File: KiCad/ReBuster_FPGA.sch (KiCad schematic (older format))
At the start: 25 parts, among them U1 10M02SCU169, U2 LM1117-3.3

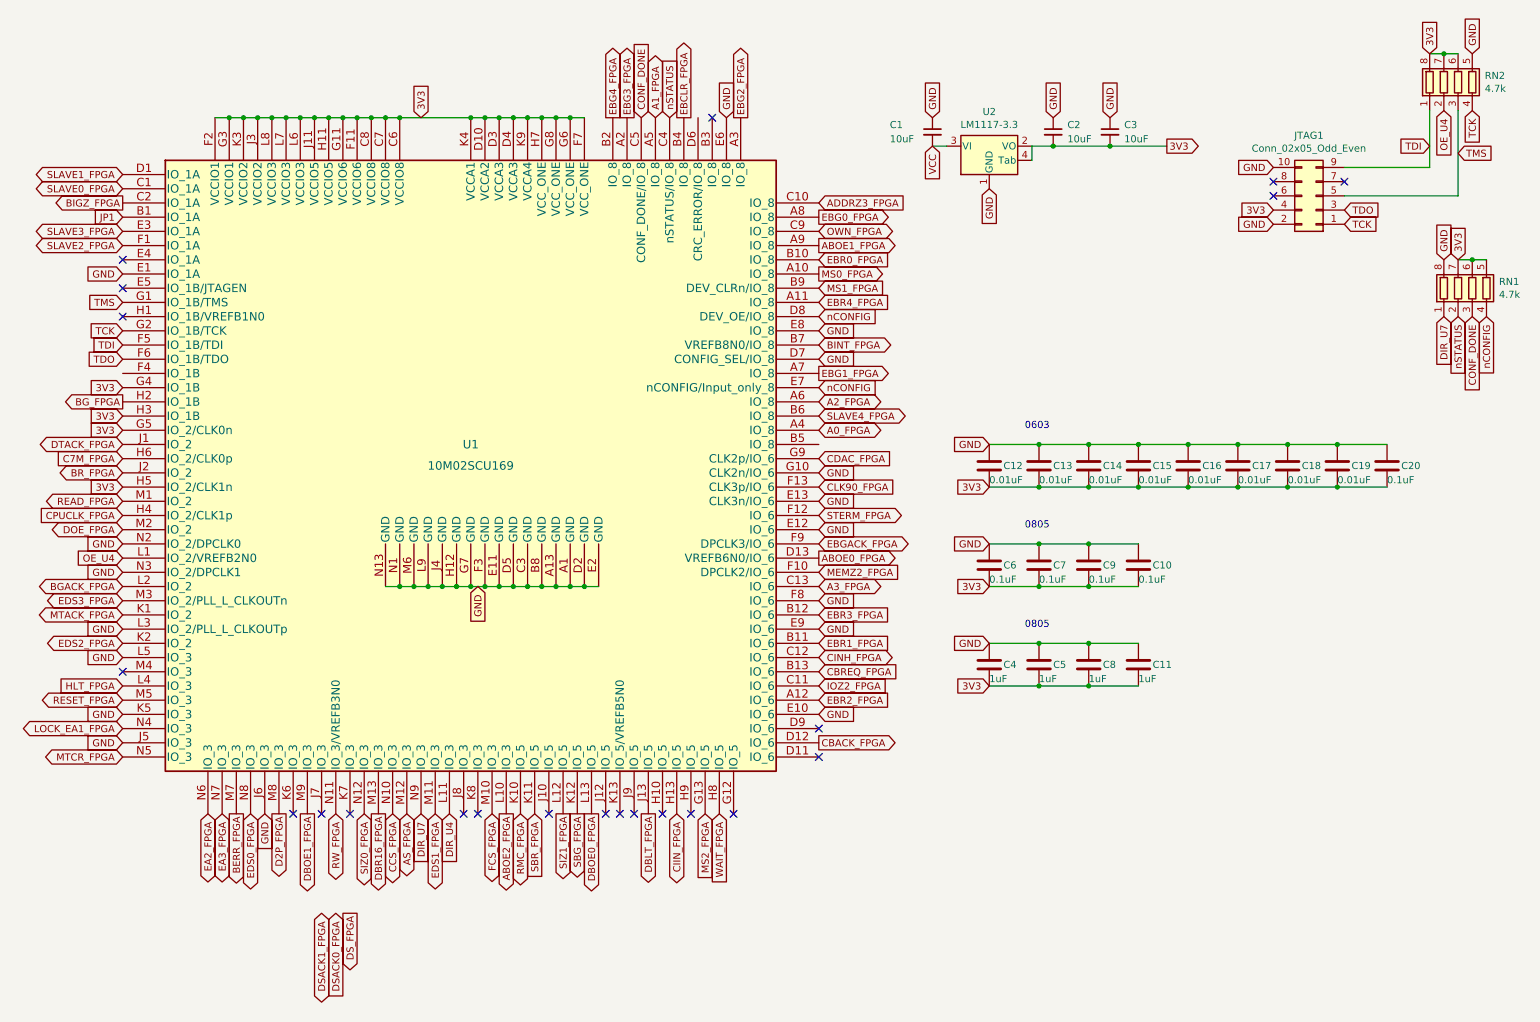
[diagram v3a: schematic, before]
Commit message: small routing fixes upgrading 0.45/0.2 mm vias to 0.5/0.3 mm where possible
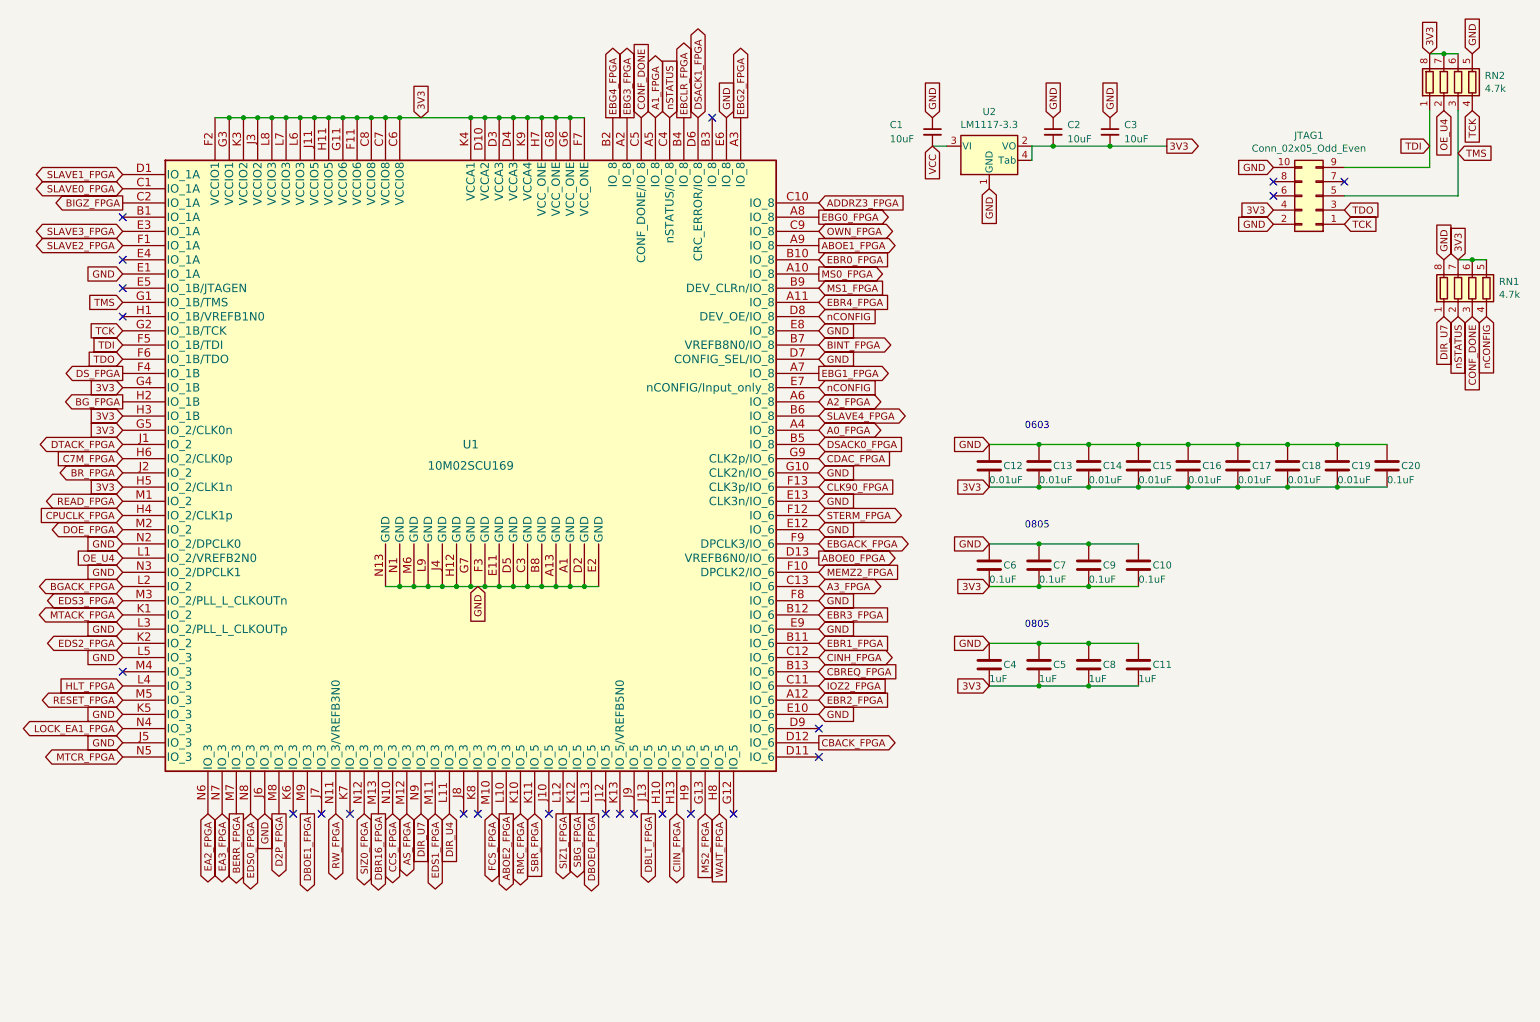
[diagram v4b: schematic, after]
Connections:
- net DSACK0_FPGA: now also U1.B5 (IO_8)
- net DSACK1_FPGA: now also U1.D6 (CRC_ERROR/IO_8)
- net DS_FPGA: now also U1.F4 (IO_1B)
- net JP1: no longer names the net of U1.B1 (IO_1A)
- no-connect marks 22 -> 23
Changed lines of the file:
@@
 Text GLabel 6050 4100 2    50   BiDi ~ 0
 STERM_FPGA
-Text GLabel 2550 6900 3    50   BiDi ~ 0
+Text GLabel 5200 1300 1    50   BiDi ~ 0
 DSACK1_FPGA
-Text GLabel 2650 6900 3    50   Input ~ 0
+Text GLabel 6050 3600 2    50   Input ~ 0
 DSACK0_FPGA
-Text GLabel 2750 6900 3    50   Output ~ 0
+Text GLabel 1150 3100 0    50   Output ~ 0
 DS_FPGA
 Text GLabel 3150 6200 3    50   BiDi ~ 0
@@
 Wire Wire Line
 	10350 850  10450 850
-Text GLabel 1150 2000 0    50   Input ~ 0
-JP1
 $Comp
 L Device:C C?
@@
 OE_U4
 NoConn ~ 4650 6200
+NoConn ~ 1150 2000
 $EndSCHEMATC

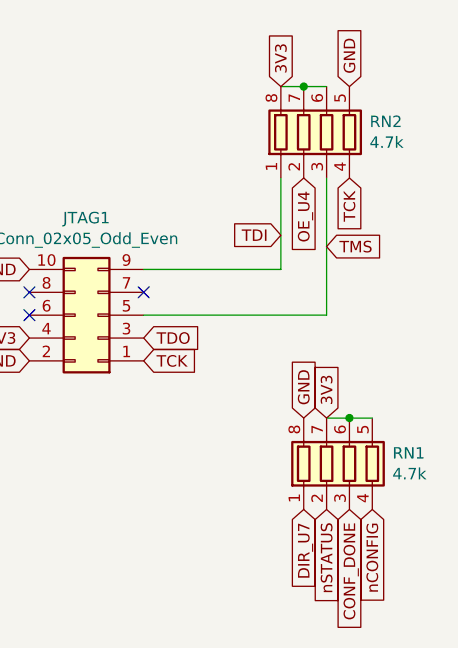
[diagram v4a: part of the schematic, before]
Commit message: Change resistor networks (RN1,RN2) to 10k Ohm
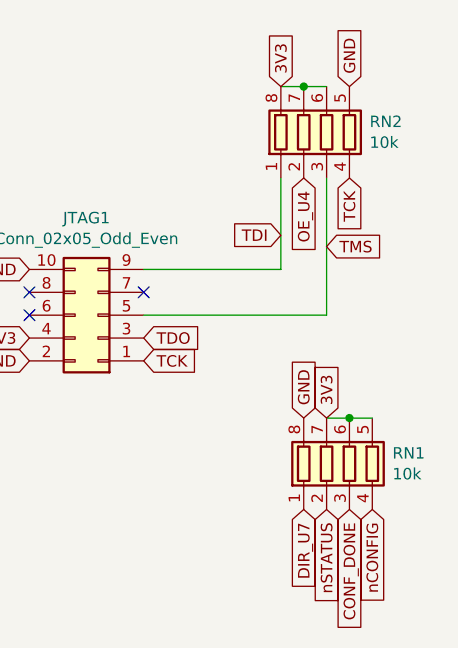
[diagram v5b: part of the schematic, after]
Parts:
- RN1, RN2: value 4.7k -> 10k
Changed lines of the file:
@@
 P 10550 1050
 F 0 "RN2" H 10738 1096 50  0000 L CNN
-F 1 "4.7k" H 10738 1005 50  0000 L CNN
+F 1 "10k" H 10738 1005 50  0000 L CNN
 F 2 "ReBuster:RESCAF80P320X160X60-8N" V 10825 1050 50  0001 C CNN
 F 3 "~" H 10550 1050 50  0001 C CNN
@@
 P 10650 2500
 F 0 "RN1" H 10838 2546 50  0000 L CNN
-F 1 "4.7k" H 10838 2455 50  0000 L CNN
+F 1 "10k" H 10838 2455 50  0000 L CNN
 F 2 "ReBuster:RESCAF80P320X160X60-8N" V 10925 2500 50  0001 C CNN
 F 3 "~" H 10650 2500 50  0001 C CNN

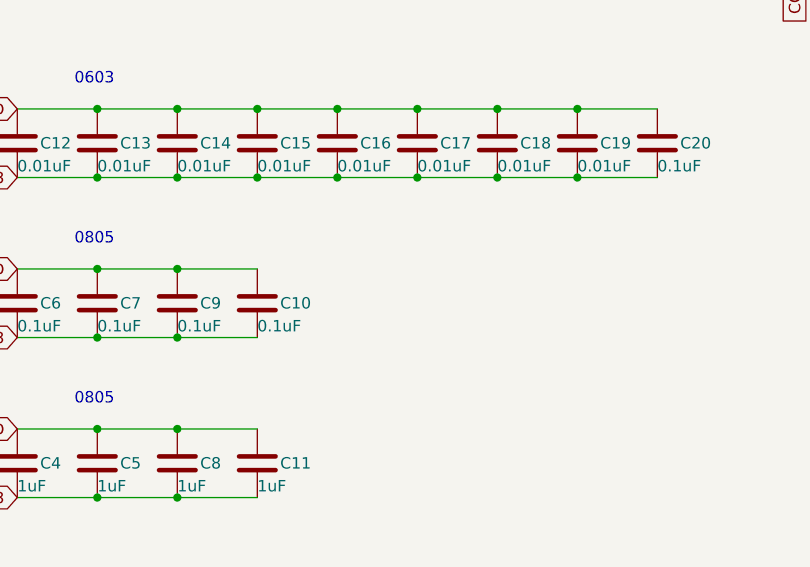
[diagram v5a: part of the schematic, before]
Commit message: Add two caps for 3.3v input pins on U4 (SN74LVC16T245DGVR)
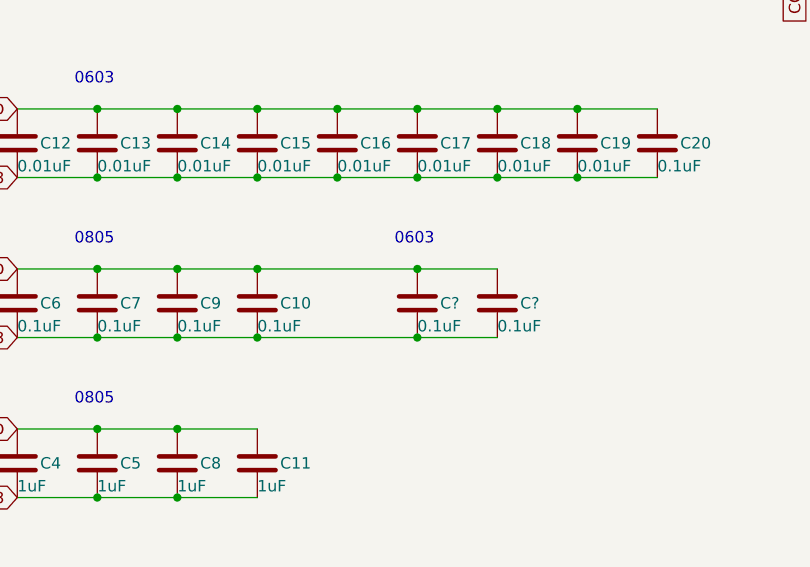
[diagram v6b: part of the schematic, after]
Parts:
- added C? (x2): 0.1uF, Capacitor_SMD:C_0603_1608Metric_Pad1.08x0.95mm_HandSolder, symbol Device:C
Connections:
- net 3V3: now also C?.2, C?.2
- net GND: now also C?.1, C?.1
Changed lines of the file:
@@
 NoConn ~ 4650 6200
 NoConn ~ 1150 2000
+$Comp
+L Device:C C?
+U 1 1 69ED3EAA
+P 9000 4450
+AR Path="/69ED3EAA" Ref="C?"  Part="1"
+AR Path="/608A10F5/69ED3EAA" Ref="C?"  Part="1"
+F 0 "C?" H 9100 4450 50  0000 L CNN
+F 1 "0.1uF" H 9000 4350 50  0000 L CNN
+F 2 "Capacitor_SMD:C_0603_1608Metric_Pad1.08x0.95mm_HandSolder" H 9038 4300 50  0001 C CNN
+F 3 "~" H 9000 4450 50  0001 C CNN
+	1    9000 4450
+	1    0    0    -1
+$EndComp
+Text Notes 8900 4200 0    50   ~ 0
+0603
+Wire Wire Line
+	8300 4300 9000 4300
+Connection ~ 8300 4300
+Wire Wire Line
+	9000 4600 8300 4600
+Connection ~ 8300 4600
+$Comp
+L Device:C C?
+U 1 1 69EDC81C
+P 9350 4450
+AR Path="/69EDC81C" Ref="C?"  Part="1"
+AR Path="/608A10F5/69EDC81C" Ref="C?"  Part="1"
+F 0 "C?" H 9450 4450 50  0000 L CNN
+F 1 "0.1uF" H 9350 4350 50  0000 L CNN
+F 2 "Capacitor_SMD:C_0603_1608Metric_Pad1.08x0.95mm_HandSolder" H 9388 4300 50  0001 C CNN
+F 3 "~" H 9350 4450 50  0001 C CNN
+	1    9350 4450
+	1    0    0    -1
+$EndComp
+Wire Wire Line
+	9000 4300 9350 4300
+Connection ~ 9000 4300
+Wire Wire Line
+	9000 4600 9350 4600
+Connection ~ 9000 4600
 $EndSCHEMATC

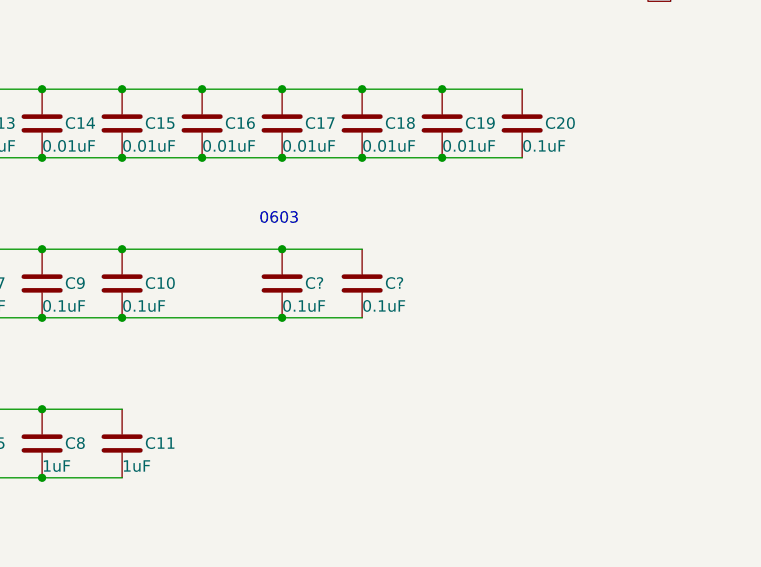
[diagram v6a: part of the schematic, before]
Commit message: Route 3.3v to U4 via caps and optimize via placements
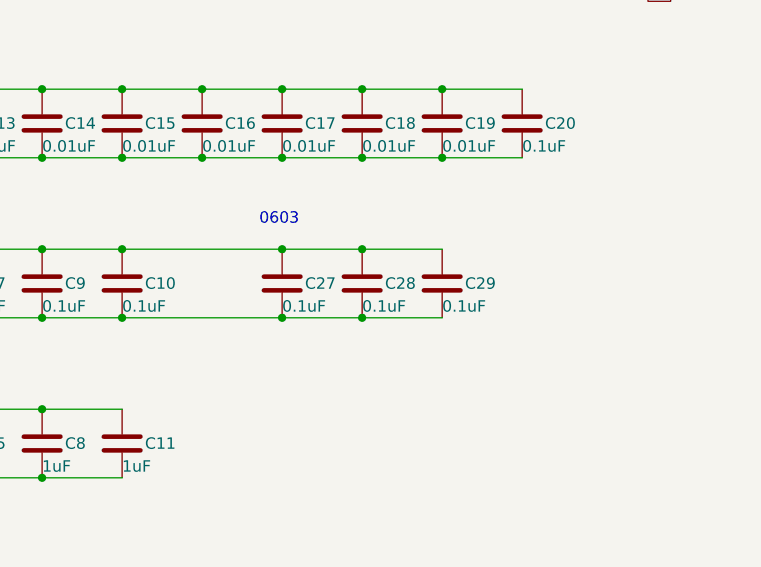
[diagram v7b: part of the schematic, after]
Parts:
- added C29: 0.1uF, ReBuster:C_0603_1608Metric_Pad1.05x0.95mm_HandSolder_extended, symbol Device:C
- gave numbers to parts that had none: 2
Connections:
- net 3V3: now also C29.2
- net GND: now also C29.1
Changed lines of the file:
@@
 P 9000 4450
 AR Path="/69ED3EAA" Ref="C?"  Part="1"
-AR Path="/608A10F5/69ED3EAA" Ref="C?"  Part="1"
-F 0 "C?" H 9100 4450 50  0000 L CNN
+AR Path="/608A10F5/69ED3EAA" Ref="C27"  Part="1"
+F 0 "C27" H 9100 4450 50  0000 L CNN
 F 1 "0.1uF" H 9000 4350 50  0000 L CNN
 F 2 "Capacitor_SMD:C_0603_1608Metric_Pad1.08x0.95mm_HandSolder" H 9038 4300 50  0001 C CNN
@@
 P 9350 4450
 AR Path="/69EDC81C" Ref="C?"  Part="1"
-AR Path="/608A10F5/69EDC81C" Ref="C?"  Part="1"
-F 0 "C?" H 9450 4450 50  0000 L CNN
+AR Path="/608A10F5/69EDC81C" Ref="C28"  Part="1"
+F 0 "C28" H 9450 4450 50  0000 L CNN
 F 1 "0.1uF" H 9350 4350 50  0000 L CNN
 F 2 "Capacitor_SMD:C_0603_1608Metric_Pad1.08x0.95mm_HandSolder" H 9388 4300 50  0001 C CNN
@@
 	9000 4600 9350 4600
 Connection ~ 9000 4600
+$Comp
+L Device:C C?
+U 1 1 69EF6B6A
+P 9700 4450
+AR Path="/69EF6B6A" Ref="C?"  Part="1"
+AR Path="/608A10F5/69EF6B6A" Ref="C29"  Part="1"
+F 0 "C29" H 9800 4450 50  0000 L CNN
+F 1 "0.1uF" H 9700 4350 50  0000 L CNN
+F 2 "ReBuster:C_0603_1608Metric_Pad1.05x0.95mm_HandSolder_extended" H 9738 4300 50  0001 C CNN
+F 3 "~" H 9700 4450 50  0001 C CNN
+	1    9700 4450
+	1    0    0    -1
+$EndComp
+Wire Wire Line
+	9350 4300 9700 4300
+Connection ~ 9350 4300
+Wire Wire Line
+	9350 4600 9700 4600
+Connection ~ 9350 4600
 $EndSCHEMATC

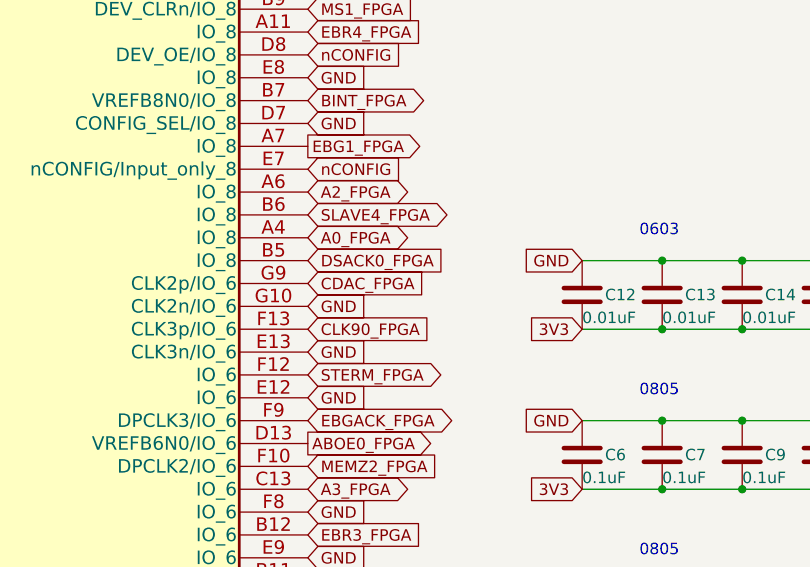
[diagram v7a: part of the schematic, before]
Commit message: remove CDAC clock (not used) and put /MTCR signal there
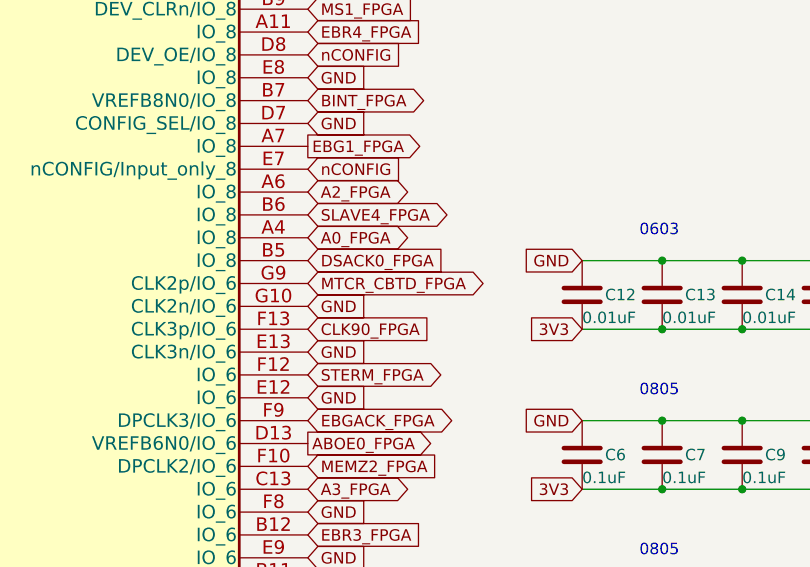
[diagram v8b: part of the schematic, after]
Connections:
- net CDAC_FPGA renamed MTCR_CBTD_FPGA
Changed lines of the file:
@@
 Text GLabel 1150 4700 0    50   BiDi ~ 0
 EDS3_FPGA
-Text GLabel 6050 3700 2    50   Input ~ 0
-CDAC_FPGA
 Text GLabel 1150 5600 0    50   BiDi ~ 0
 LOCK_EA1_FPGA
@@
 	9350 4600 9700 4600
 Connection ~ 9350 4600
+Text GLabel 6050 3700 2    50   BiDi ~ 0
+MTCR_CBTD_FPGA
 $EndSCHEMATC
